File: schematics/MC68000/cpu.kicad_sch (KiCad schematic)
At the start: 58 parts, among them J2 Conn_02x37_Row_Letter_Last, SW1 Reset, U1 74LS00, U10 74LS244, U11 74LS244, U12 74LS148, U2 74LS05, U3 74LS161, U4 ICM7555xB, U5 68000D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

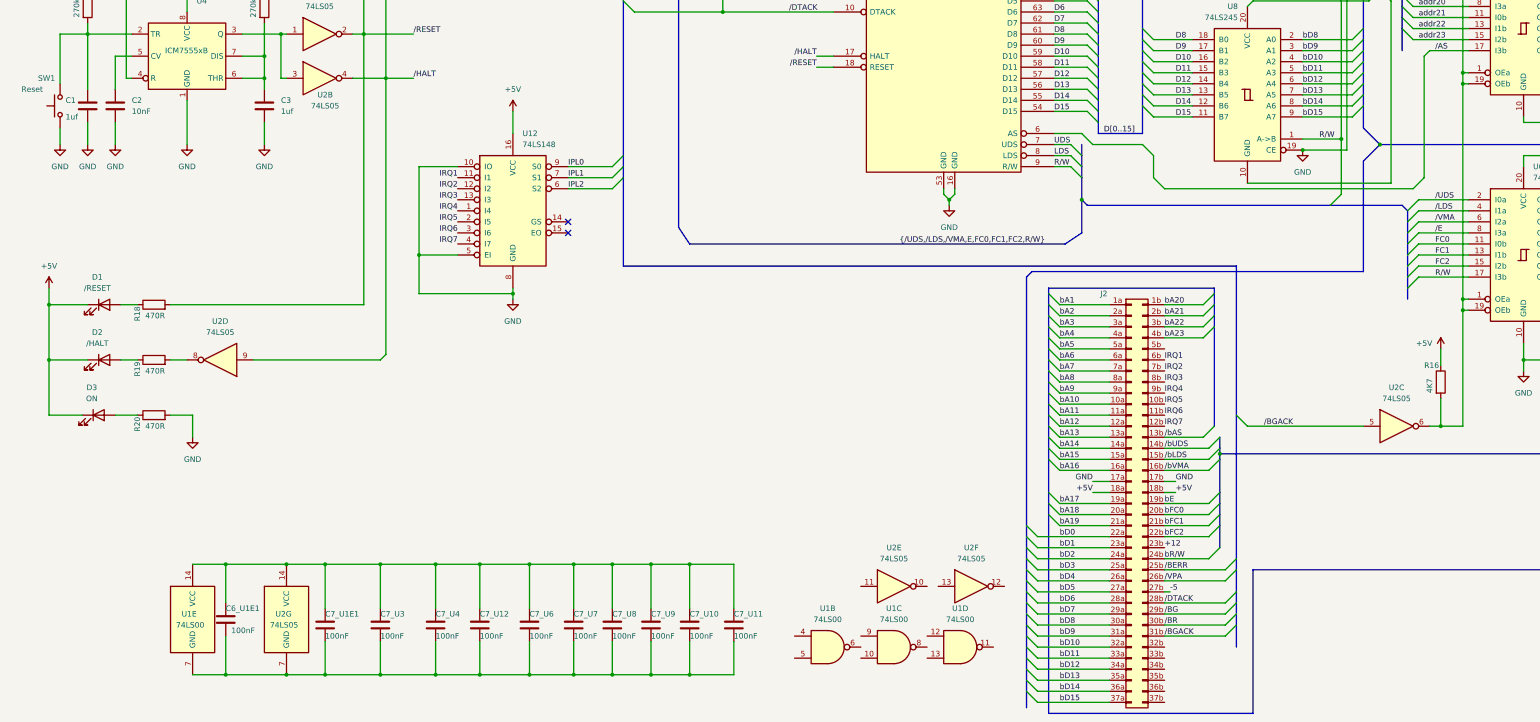
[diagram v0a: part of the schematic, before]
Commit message: cleanup zips and added memory map equations for pld
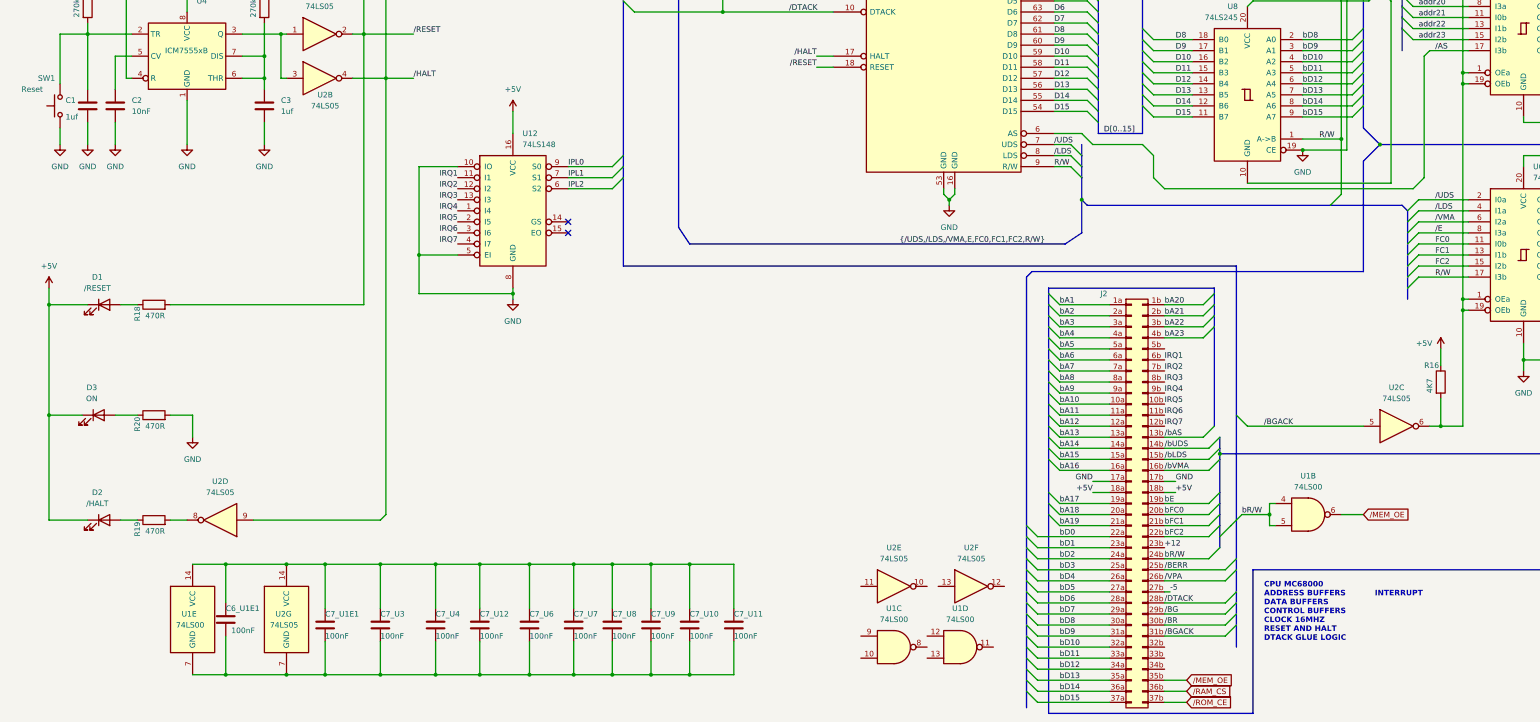
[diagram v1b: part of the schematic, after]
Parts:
- C1, C3: footprint (none) -> Capacitor_THT:CP_Radial_D8.0mm_P3.50mm
- C2: footprint (none) -> Capacitor_SMD:C_0603_1608Metric
- C4_U5, C5_U5: footprint (none) -> Capacitor_THT:C_Disc_D4.3mm_W1.9mm_P5.00mm
- D1, D2, D3: footprint (none) -> Diode_THT:D_DO-34_SOD68_P5.08mm_Vertical_AnodeUp
- J2: footprint (none) -> Connector_PinHeader_2.54mm:PinHeader_2x37_P2.54mm_Vertical
- JP1, JP2, JP3, JP4: footprint (none) -> Connector_PinHeader_2.54mm:PinHeader_1x02_P2.54mm_Vertical
- R1, R10, R11, R12, R13, R14, R15, R16, R17, R18, R19, R2, R20, R3, R4, R5, R6, R7, R8, R9: footprint (none) -> Resistor_THT:R_Axial_DIN0204_L3.6mm_D1.6mm_P5.08mm_Horizontal
- SW1: footprint (none) -> Button_Switch_THT:SW_Push_1P2T_Vertical_E-Switch_800UDP8P1A1M6
- U1, U2: footprint (none) -> Package_DIP:CERDIP-14_W7.62mm_SideBrazed_LongPads
- U10, U11, U6, U7, U8, U9: footprint (none) -> Package_DIP:CERDIP-20_W7.62mm_SideBrazed_LongPads
- U12, U3: footprint (none) -> Package_DIP:CERDIP-16_W7.62mm_SideBrazed_LongPads
- U5: footprint (none) -> Package_DIP:DIP-64_W22.86mm
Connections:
- net LDS is gone; now on net /LDS: U5.8 (LDS)
- net UDS is gone; now on net /UDS: U5.7 (UDS)
- net bR/W: now also U1.4, U1.5
- net /RAM_CS: now also J2.36b (Pin_36b)
- net /ROM_CE: now also J2.37b (Pin_37b)
- net /MEM_OE: now reaches J2.35b (Pin_35b)
- net /MEM_OE: now also U1.6
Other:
- note added: "CPU MC68000 ADDRESS BUFFERS INTERRUPT DATA BUFFERS CONTROL BUFFERS CLOCK 16MHZ RESET AND HALT DTACK GLUE LOGIC"
- moved on the sheet: D2, R19, U1B, U2D

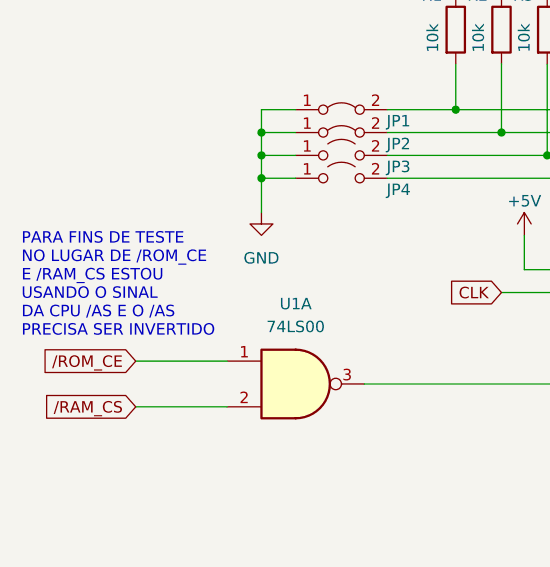
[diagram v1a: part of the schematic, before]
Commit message: Cpu's board tested
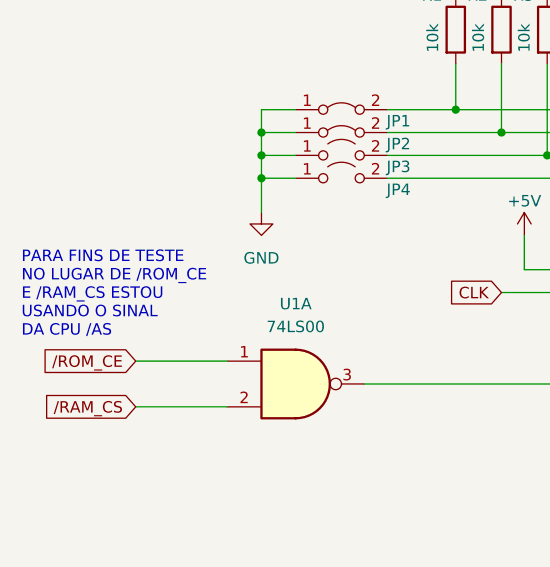
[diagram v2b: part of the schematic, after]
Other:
- note added: "PARA FINS DE TESTE NO LUGAR DE /ROM_CE E /RAM_CS ESTOU USANDO O SINAL DA CPU /AS"
- note removed: "PARA FINS DE TESTE NO LUGAR DE /ROM_CE E /RAM_CS ESTOU USANDO O SINAL DA CPU /AS E O /AS PRECISA SER INVERTIDO"
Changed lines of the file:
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@@
     (effects (font (size 1.27 1.27) (thickness 0.254) bold) (justify left bottom))
   )
-  (text "PARA FINS DE TESTE\nNO LUGAR DE /ROM_CE\nE /RAM_CS ESTOU \nUSANDO O SINAL \nDA CPU /AS E O /AS\nPRECISA SER INVERTIDO\n"
+  (text "PARA FINS DE TESTE\nNO LUGAR DE /ROM_CE\nE /RAM_CS ESTOU \nUSANDO O SINAL \nDA CPU /AS "
     (at 12.7 77.47 0)
     (effects (font (size 1.27 1.27)) (justify left bottom))

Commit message: Ram memory test 2 OK
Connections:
- net bR/W: now also U2.11
- net /DTACK: now also J2.35b (Pin_35b); no longer J2.28b (Pin_28b)
- net /MEM_OE: no longer J2.35b (Pin_35b)
- net /RAM_CS: no longer J2.36b (Pin_36b)
- net /RESET: now also J2.37b (Pin_37b)
- net /ROM_CE: no longer J2.37b (Pin_37b)
- net /RD: now reaches J2.33b (Pin_33b)
- net /RD: now also U2.10
- net /IO_CS: now reaches J2.34b (Pin_34b)
- new net RESET: J2.36b (Pin_36b)
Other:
- moved on the sheet: U2E
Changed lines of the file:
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@@
     (stroke (width 0) (type default))
   )
-  (bus_entry (at 294.64 256.54) (size -2.54 2.54)
-    (stroke (width 0) (type default))
-  )
   (bus_entry (at 262.89 113.03) (size -2.54 -2.54)
     (stroke (width 0) (type default))
@@
     (stroke (width 0) (type default))
   )
+  (wire (pts (xy 283.21 271.78) (xy 278.13 271.78))
+    (stroke (width 0) (type default))
+  )
   (wire (pts (xy 335.28 31.75) (xy 347.98 31.75))
     (stroke (width 0) (type default))
@@
     (stroke (width 0) (type default))
   )
-  (wire (pts (xy 292.1 259.08) (xy 278.13 259.08))
-    (stroke (width 0) (type default))
-  )
   (bus (pts (xy 259.08 153.67) (xy 259.08 156.21))
     (stroke (width 0) (type default))
@@
     (stroke (width 0) (type default))
   )
+  (wire (pts (xy 283.21 274.32) (xy 278.13 274.32))
+    (stroke (width 0) (type default))
+  )
   (wire (pts (xy 36.83 133.35) (xy 36.83 140.97))
     (stroke (width 0) (type default))
@@
     (effects (font (size 1.27 1.27)) (justify left bottom))
   )
+  (label "bR{slash}W" (at 213.36 231.14 180) (fields_autoplaced)
+    (effects (font (size 1.27 1.27)) (justify right bottom))
+  )
   (label "bA7" (at 373.38 41.91 0) (fields_autoplaced)
     (effects (font (size 1.27 1.27)) (justify left bottom))
@@
     (effects (font (size 1.27 1.27)) (justify left bottom))
   )
+  (label "{slash}RD" (at 228.6 231.14 0) (fields_autoplaced)
+    (effects (font (size 1.27 1.27)) (justify left bottom))
+  )
   (label "bD5" (at 309.88 97.79 0) (fields_autoplaced)
     (effects (font (size 1.27 1.27)) (justify left bottom))
@@
     (effects (font (size 1.27 1.27)) (justify left bottom))
   )
-  (label "{slash}DTACK" (at 278.13 259.08 0) (fields_autoplaced)
-    (effects (font (size 1.27 1.27)) (justify left bottom))
-  )
   (label "addr8" (at 252.73 64.77 0) (fields_autoplaced)
     (effects (font (size 1.27 1.27)) (justify left bottom))
@@
     (effects (font (size 1.27 1.27)) (justify left bottom))
   )
-  (global_label "{slash}ROM_CE" (shape input) (at 283.21 281.94 0) (fields_autoplaced)
+  (global_label "{slash}RD" (shape input) (at 283.21 271.78 0) (fields_autoplaced)
     (effects (font (size 1.27 1.27)) (justify left))
-    (property "Intersheetrefs" "${INTERSHEET_REFS}" (at 294.9642 281.94 0)
+    (property "Intersheetrefs" "${INTERSHEET_REFS}" (at 290.0657 271.78 0)
       (effects (font (size 1.27 1.27)) (justify left) hide)
     )
   )
-  (global_label "{slash}MEM_OE" (shape input) (at 283.21 276.86 0) (fields_autoplaced)
+  (global_label "{slash}RESET" (shape input) (at 283.21 281.94 0) (fields_autoplaced)
     (effects (font (size 1.27 1.27)) (justify left))
-    (property "Intersheetrefs" "${INTERSHEET_REFS}" (at 295.0246 276.86 0)
+    (property "Intersheetrefs" "${INTERSHEET_REFS}" (at 293.2708 281.94 0)
+      (effects (font (size 1.27 1.27)) (justify left) hide)
+    )
+  )
+  (global_label "{slash}DTACK" (shape input) (at 283.21 276.86 0) (fields_autoplaced)
+    (effects (font (size 1.27 1.27)) (justify left))
+    (property "Intersheetrefs" "${INTERSHEET_REFS}" (at 293.3919 276.86 0)
       (effects (font (size 1.27 1.27)) (justify left) hide)
     )
@@
     )
   )
+  (global_label "{slash}IO_CS" (shape input) (at 283.21 274.32 0) (fields_autoplaced)
+    (effects (font (size 1.27 1.27)) (justify left))
+    (property "Intersheetrefs" "${INTERSHEET_REFS}" (at 292.9081 274.32 0)
+      (effects (font (size 1.27 1.27)) (justify left) hide)
+    )
+  )
   (global_label "{slash}MEM_OE" (shape input) (at 323.85 238.76 0) (fields_autoplaced)
     (effects (font (size 1.27 1.27)) (justify left))
@@
     )
   )
-  (global_label "{slash}RAM_CS" (shape input) (at 283.21 279.4 0) (fields_autoplaced)
+  (global_label "RESET" (shape input) (at 283.21 279.4 0) (fields_autoplaced)
     (effects (font (size 1.27 1.27)) (justify left))
-    (property "Intersheetrefs" "${INTERSHEET_REFS}" (at 294.7828 279.4 0)
+    (property "Intersheetrefs" "${INTERSHEET_REFS}" (at 291.9403 279.4 0)
       (effects (font (size 1.27 1.27)) (justify left) hide)
     )
@@
     )
   )
-  (symbol (lib_id "74xx:74LS05") (at 215.9 255.27 0) (unit 5)
+  (symbol (lib_id "74xx:74LS05") (at 220.98 231.14 0) (unit 5)
     (in_bom yes) (on_board yes) (dnp no) (fields_autoplaced)
-    (property "Reference" "U2" (at 215.9 246.38 0)
+    (property "Reference" "U2" (at 220.98 222.25 0)
       (effects (font (size 1.27 1.27)))
     )
-    (property "Value" "74LS05" (at 215.9 248.92 0)
+    (property "Value" "74LS05" (at 220.98 224.79 0)
       (effects (font (size 1.27 1.27)))
     )
-    (property "Footprint" "Package_DIP:CERDIP-14_W7.62mm_SideBrazed_LongPads" (at 215.9 255.27 0)
+    (property "Footprint" "Package_DIP:CERDIP-14_W7.62mm_SideBrazed_LongPads" (at 220.98 231.14 0)
       (effects (font (size 1.27 1.27)) hide)
     )
-    (property "Datasheet" "http://www.ti.com/lit/gpn/sn74LS05" (at 215.9 255.27 0)
+    (property "Datasheet" "http://www.ti.com/lit/gpn/sn74LS05" (at 220.98 231.14 0)
       (effects (font (size 1.27 1.27)) hide)
     )
